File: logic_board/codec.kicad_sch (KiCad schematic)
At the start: 1 part, among them U2 WM8904CGEFL/V

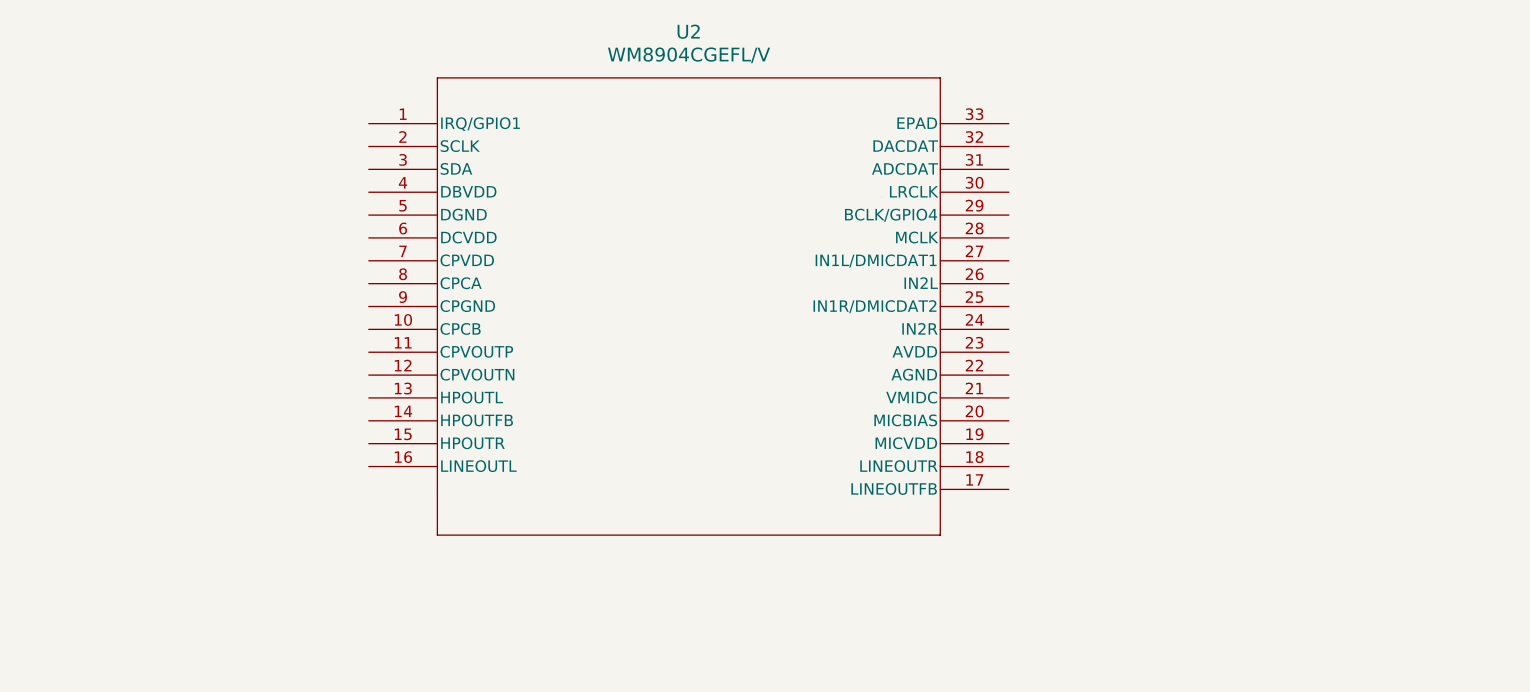
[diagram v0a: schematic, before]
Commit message: Create a pin mapping file
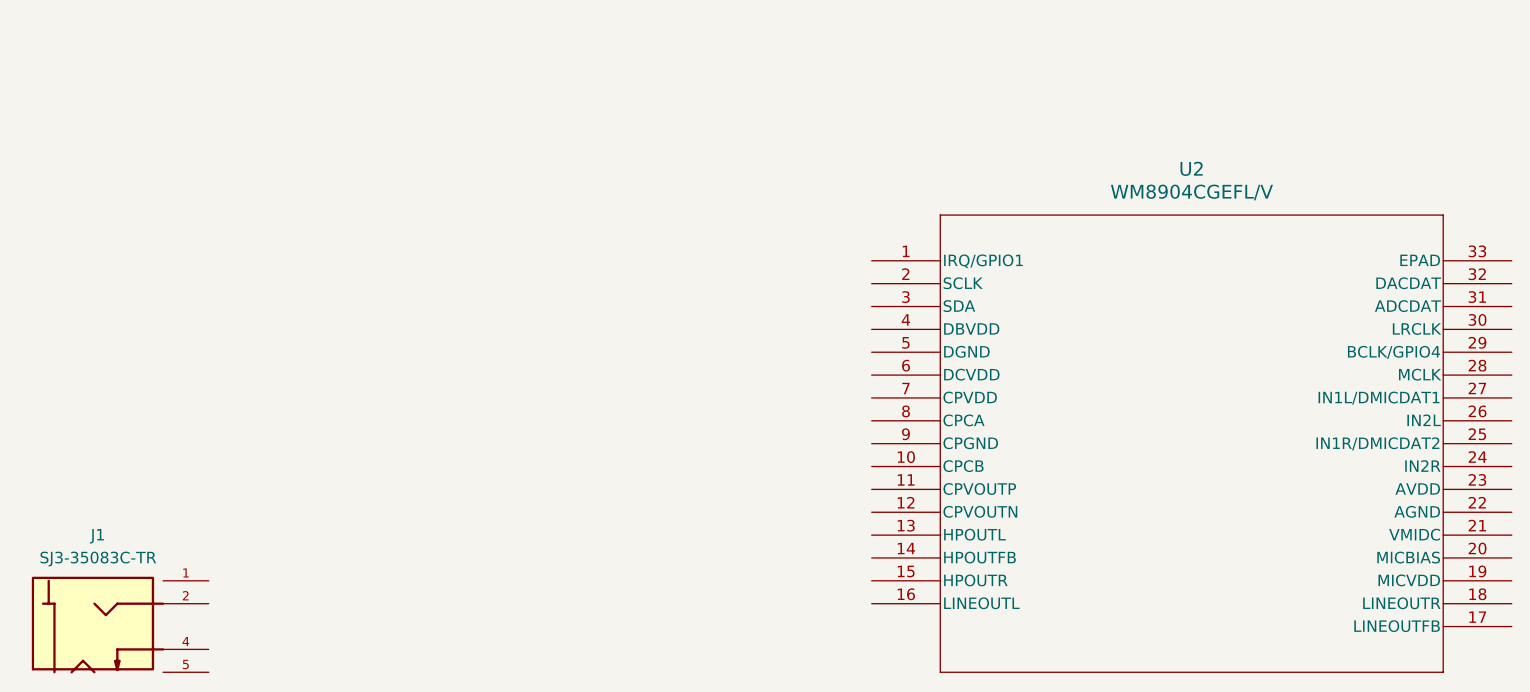
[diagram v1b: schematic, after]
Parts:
- added J1: SJ3-35083C-TR, Custom_Footprints:SAMESKY_SJ3-35083C-TR, symbol Custom_Symbols:SJ3-35083C-TR
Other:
- moved on the sheet: U2
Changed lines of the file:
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@@
 	(paper "A4")
 	(symbol
+		(lib_id "Custom_Symbols:SJ3-35083C-TR")
+		(at 49.53 109.22 0)
+		(unit 1)
+		(exclude_from_sim no)
+		(in_bom no)
+		(on_board yes)
+		(dnp no)
+		(fields_autoplaced yes)
+		(property "Reference" "J1"
+			(at 47.3834 99.06 0)
+			(effects
+				(font
+					(size 1.27 1.27)
+				)
+			)
+		)
+		(property "Value" "SJ3-35083C-TR"
+			(at 47.3834 101.6 0)
+			(effects
+				(font
+					(size 1.27 1.27)
+				)
+			)
+		)
+		(property "Footprint" "Custom_Footprints:SAMESKY_SJ3-35083C-TR"
+			(at 49.53 109.22 0)
+			(effects
+				(font
+					(size 1.27 1.27)
+				)
+				(justify bottom)
+				(hide yes)
+			)
+		)
+		(property "Datasheet" "https://www.sameskydevices.com/product/resource/sj3-3508x.pdf"
+			(at 49.53 109.22 0)
+			(effects
+				(font
+					(size 1.27 1.27)
+				)
+				(hide yes)
+			)
+		)
+		(property "Description" "3.5mm Audio Jack"
+			(at 49.53 109.22 0)
+			(effects
+				(font
+					(size 1.27 1.27)
+				)
+				(hide yes)
+			)
+		)
+		(property "PARTREV" "1.01"
+			(at 49.53 109.22 0)
+			(effects
+				(font
+					(size 1.27 1.27)
+				)
+				(justify bottom)
+				(hide yes)
+			)
+		)
+		(property "STANDARD" "Manufacturer Recommendations"
+			(at 49.53 109.22 0)
+			(effects
+				(font
+					(size 1.27 1.27)
+				)
+				(justify bottom)
+				(hide yes)
+			)
+		)
+		(property "MAXIMUM_PACKAGE_HEIGHT" "5.3mm"
+			(at 49.53 109.22 0)
+			(effects
+				(font
+					(size 1.27 1.27)
+				)
+				(justify bottom)
+				(hide yes)
+			)
+		)
+		(property "MANUFACTURER" "Same Sky"
+			(at 49.53 109.22 0)
+			(effects
+				(font
+					(size 1.27 1.27)
+				)
+				(justify bottom)
+				(hide yes)
+			)
+		)
+		(pin "1"
+		)
+		(pin "2"
+		)
+		(pin "4"
+		)
+		(pin "5"
+		)
+		(instances
+			(project "logic_board"
+				(path "/b7b37fe1-b409-497a-9440-d94d882f6459/824f357b-6dd3-4dc3-a0f3-1ff6a8c5aeec"
+					(reference "J1")
+					(unit 1)
+				)
+			)
+		)
+	)
+	(symbol
 		(lib_id "Custom_Symbols:WM8904CGEFL_V")
-		(at 77.47 53.34 0)
+		(at 133.35 68.58 0)
 		(unit 1)
 		(exclude_from_sim no)
@@
 		(fields_autoplaced yes)
 		(property "Reference" "U2"
-			(at 113.03 43.18 0)
+			(at 168.91 58.42 0)
 			(effects
 				(font
@@
 		)
 		(property "Value" "WM8904CGEFL/V"
-			(at 113.03 45.72 0)
+			(at 168.91 60.96 0)
 			(effects
 				(font
@@
 		)
 		(property "Footprint" "Custom_Footprints:QFN32_4X4_CIR"
-			(at 77.47 53.34 0)
+			(at 133.35 68.58 0)
 			(effects
 				(font
@@
 			)
 		)
-		(property "Datasheet" "WM8904CGEFL/V"
-			(at 77.47 53.34 0)
+		(property "Datasheet" "https://statics.cirrus.com/pubs/proDatasheet/WM8904_Rev4.0.pdf"
+			(at 133.35 68.58 0)
 			(effects
 				(font
@@
 			)
 		)
-		(property "Description" ""
-			(at 77.47 53.34 0)
+		(property "Description" "Audio Codec"
+			(at 133.35 68.58 0)
 			(effects
 				(font
@@
 		)
 		(property "LCSC Part Number" "C1521513"
-			(at 77.47 53.34 0)
+			(at 133.35 68.58 0)
 			(effects
 				(font

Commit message: Add more parts to schematic
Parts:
- added J4: AudioPlug2, Connector_Wire:SolderWire-0.5sqmm_1x02_P4.6mm_D0.9mm_OD2.1mm, symbol Connector_Audio:AudioPlug2
- added U6: TLV9061xDBV, Package_TO_SOT_SMD:SOT-23-5, symbol Amplifier_Operational:TLV9061xDBV
- J1: LCSC Part Number (none) -> C9900193904
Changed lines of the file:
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@@
+			)
+		)
+		(property "LCSC Part Number" "C9900193904"
+			(at 49.53 109.22 0)
+			(effects
+				(font
+					(size 1.27 1.27)
+				)
+				(hide yes)
 			)
 		)
@@
 					(unit 1)
 				)
+			)
+		)
+	)
+	(symbol
+		(lib_id "Connector_Audio:AudioPlug2")
+		(at 35.56 73.66 0)
+		(unit 1)
+		(exclude_from_sim no)
+		(in_bom no)
+		(on_board yes)
+		(dnp no)
+		(fields_autoplaced yes)
+		(property "Reference" "J4"
+			(at 35.56 63.5 0)
+			(effects
+				(font
+					(size 1.27 1.27)
+				)
+			)
+		)
+		(property "Value" "AudioPlug2"
+			(at 35.56 66.04 0)
+			(effects
+				(font
+					(size 1.27 1.27)
+				)
+			)
+		)
+		(property "Footprint" "Connector_Wire:SolderWire-0.5sqmm_1x02_P4.6mm_D0.9mm_OD2.1mm"
+			(at 44.45 74.93 0)
+			(effects
+				(font
+					(size 1.27 1.27)
+				)
+				(hide yes)
+			)
+		)
+		(property "Datasheet" "~"
+			(at 44.45 74.93 0)
+			(effects
+				(font
+					(size 1.27 1.27)
+				)
+				(hide yes)
+			)
+		)
+		(property "Description" "Audio Jack, 2 Poles (Mono / TS)"
+			(at 35.56 73.66 0)
+			(effects
+				(font
+					(size 1.27 1.27)
+				)
+				(hide yes)
+			)
+		)
+		(pin "S"
+		)
+		(pin "T"
+		)
+		(instances
+			(project ""
+				(path "/b7b37fe1-b409-497a-9440-d94d882f6459/824f357b-6dd3-4dc3-a0f3-1ff6a8c5aeec"
+					(reference "J4")
+					(unit 1)
+				)
+			)
+		)
+	)
+	(symbol
+		(lib_id "Amplifier_Operational:TLV9061xDBV")
+		(at 68.58 50.8 0)
+		(unit 1)
+		(exclude_from_sim no)
+		(in_bom yes)
+		(on_board yes)
+		(dnp no)
+		(fields_autoplaced yes)
+		(property "Reference" "U6"
+			(at 81.28 44.3798 0)
+			(effects
+				(font
+					(size 1.27 1.27)
+				)
+			)
+		)
+		(property "Value" "TLV9061xDBV"
+			(at 81.28 46.9198 0)
+			(effects
+				(font
+					(size 1.27 1.27)
+				)
+			)
+		)
+		(property "Footprint" "Package_TO_SOT_SMD:SOT-23-5"
+			(at 53.34 69.85 0)
+			(effects
+				(font
+					(size 1.27 1.27)
+				)
+				(justify left)
+				(hide yes)
+			)
+		)
+		(property "Datasheet" "https://www.ti.com/lit/ds/symlink/tlv9061.pdf"
+			(at 68.58 30.48 0)
+			(effects
+				(font
+					(size 1.27 1.27)
+				)
+				(hide yes)
+			)
+		)
+		(property "Description" "10-MHz, RRIO, CMOS Operational Amplifiers for Cost-Sensitive Systems, SOT-23-5"
+			(at 68.58 50.8 0)
+			(effects
+				(font
+					(size 1.27 1.27)
+				)
+				(hide yes)
+			)
+		)
+		(property "LCSC Part Number" "C398358"
+			(at 68.58 50.8 0)
+			(effects
+				(font
+					(size 1.27 1.27)
+				)
+				(hide yes)
+			)
+		)
+		(pin "1"
+		)
+		(pin "3"
+		)
+		(pin "5"
+		)
+		(pin "4"
+		)
+		(pin "2"
+		)
+		(instances
+			(project ""
+				(path "/b7b37fe1-b409-497a-9440-d94d882f6459/824f357b-6dd3-4dc3-a0f3-1ff6a8c5aeec"
+					(reference "U6")
+					(unit 1)
+				)

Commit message: Board and symbol updates.
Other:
- moved on the sheet: J4, U6
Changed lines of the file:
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@@
 	(symbol
 		(lib_id "Custom_Symbols:SJ3-35083C-TR")
-		(at 49.53 109.22 0)
+		(at 80.01 107.95 0)
 		(unit 1)
 		(exclude_from_sim no)
@@
 		(fields_autoplaced yes)
 		(property "Reference" "J1"
-			(at 47.3834 99.06 0)
+			(at 77.8634 97.79 0)
 			(effects
 				(font
@@
 		)
 		(property "Value" "SJ3-35083C-TR"
-			(at 47.3834 101.6 0)
+			(at 77.8634 100.33 0)
 			(effects
 				(font
@@
 		)
 		(property "Footprint" "Custom_Footprints:SAMESKY_SJ3-35083C-TR"
-			(at 49.53 109.22 0)
+			(at 80.01 107.95 0)
 			(effects
 				(font
@@
 		)
 		(property "Datasheet" "https://www.sameskydevices.com/product/resource/sj3-3508x.pdf"
-			(at 49.53 109.22 0)
+			(at 80.01 107.95 0)
 			(effects
 				(font
@@
 		)
 		(property "Description" "3.5mm Audio Jack"
-			(at 49.53 109.22 0)
+			(at 80.01 107.95 0)
 			(effects
 				(font
@@
 		)
 		(property "PARTREV" "1.01"
-			(at 49.53 109.22 0)
+			(at 80.01 107.95 0)
 			(effects
 				(font
@@
 		)
 		(property "STANDARD" "Manufacturer Recommendations"
-			(at 49.53 109.22 0)
+			(at 80.01 107.95 0)
 			(effects
 				(font
@@
 		)
 		(property "MAXIMUM_PACKAGE_HEIGHT" "5.3mm"
-			(at 49.53 109.22 0)
+			(at 80.01 107.95 0)
 			(effects
 				(font
@@
 		)
 		(property "MANUFACTURER" "Same Sky"
-			(at 49.53 109.22 0)
+			(at 80.01 107.95 0)
 			(effects
 				(font
@@
 		)
 		(property "LCSC Part Number" "C9900193904"
-			(at 49.53 109.22 0)
+			(at 80.01 107.95 0)
 			(effects
 				(font
@@
 	(symbol
 		(lib_id "Connector_Audio:AudioPlug2")
-		(at 35.56 73.66 0)
+		(at 40.64 59.69 0)
 		(unit 1)
 		(exclude_from_sim no)
@@
 		(fields_autoplaced yes)
 		(property "Reference" "J4"
-			(at 35.56 63.5 0)
+			(at 40.64 49.53 0)
 			(effects
 				(font
@@
 		)
 		(property "Value" "AudioPlug2"
-			(at 35.56 66.04 0)
+			(at 40.64 52.07 0)
 			(effects
 				(font
@@
 		)
 		(property "Footprint" "Connector_Wire:SolderWire-0.5sqmm_1x02_P4.6mm_D0.9mm_OD2.1mm"
-			(at 44.45 74.93 0)
+			(at 49.53 60.96 0)
 			(effects
 				(font
@@
 		)
 		(property "Datasheet" "~"
-			(at 44.45 74.93 0)
+			(at 49.53 60.96 0)
 			(effects
 				(font
@@
 		)
 		(property "Description" "Audio Jack, 2 Poles (Mono / TS)"
-			(at 35.56 73.66 0)
+			(at 40.64 59.69 0)
 			(effects
 				(font
@@
 	(symbol
 		(lib_id "Amplifier_Operational:TLV9061xDBV")
-		(at 68.58 50.8 0)
+		(at 77.47 58.42 0)
 		(unit 1)
 		(exclude_from_sim no)
@@
 		(fields_autoplaced yes)
 		(property "Reference" "U6"
-			(at 81.28 44.3798 0)
+			(at 90.17 51.9998 0)
 			(effects
 				(font
@@
 		)
 		(property "Value" "TLV9061xDBV"
-			(at 81.28 46.9198 0)
+			(at 90.17 54.5398 0)
 			(effects
 				(font
@@
 		)
 		(property "Footprint" "Package_TO_SOT_SMD:SOT-23-5"
-			(at 53.34 69.85 0)
+			(at 62.23 77.47 0)
 			(effects
 				(font
@@
 		)
 		(property "Datasheet" "https://www.ti.com/lit/ds/symlink/tlv9061.pdf"
-			(at 68.58 30.48 0)
+			(at 77.47 38.1 0)
 			(effects
 				(font
@@
 		)
 		(property "Description" "10-MHz, RRIO, CMOS Operational Amplifiers for Cost-Sensitive Systems, SOT-23-5"
-			(at 68.58 50.8 0)
+			(at 77.47 58.42 0)
 			(effects
 				(font
@@
 		)
 		(property "LCSC Part Number" "C398358"
-			(at 68.58 50.8 0)
-			(effects
-				(font
+			(at 77.47 58.42 0)
+			(effects
+				(font

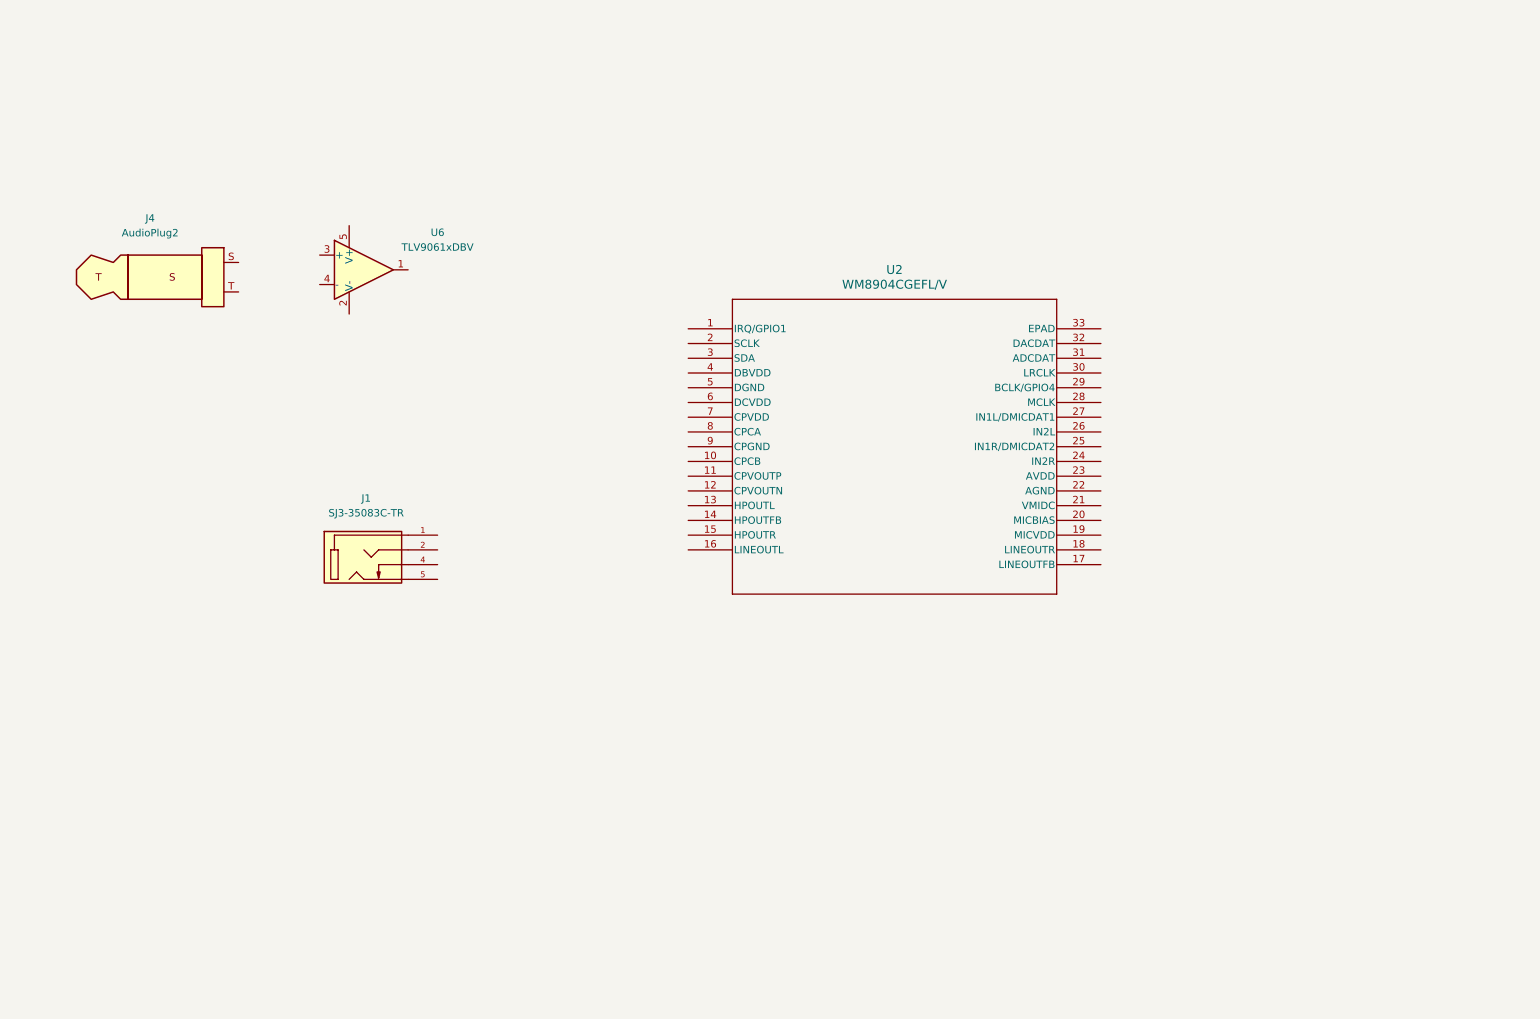
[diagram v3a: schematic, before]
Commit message: Ready for routing. - Lay out all components in proper positions - Add all support passives (bypass caps, etc) - Add board corner cutouts for enclosure bosses.
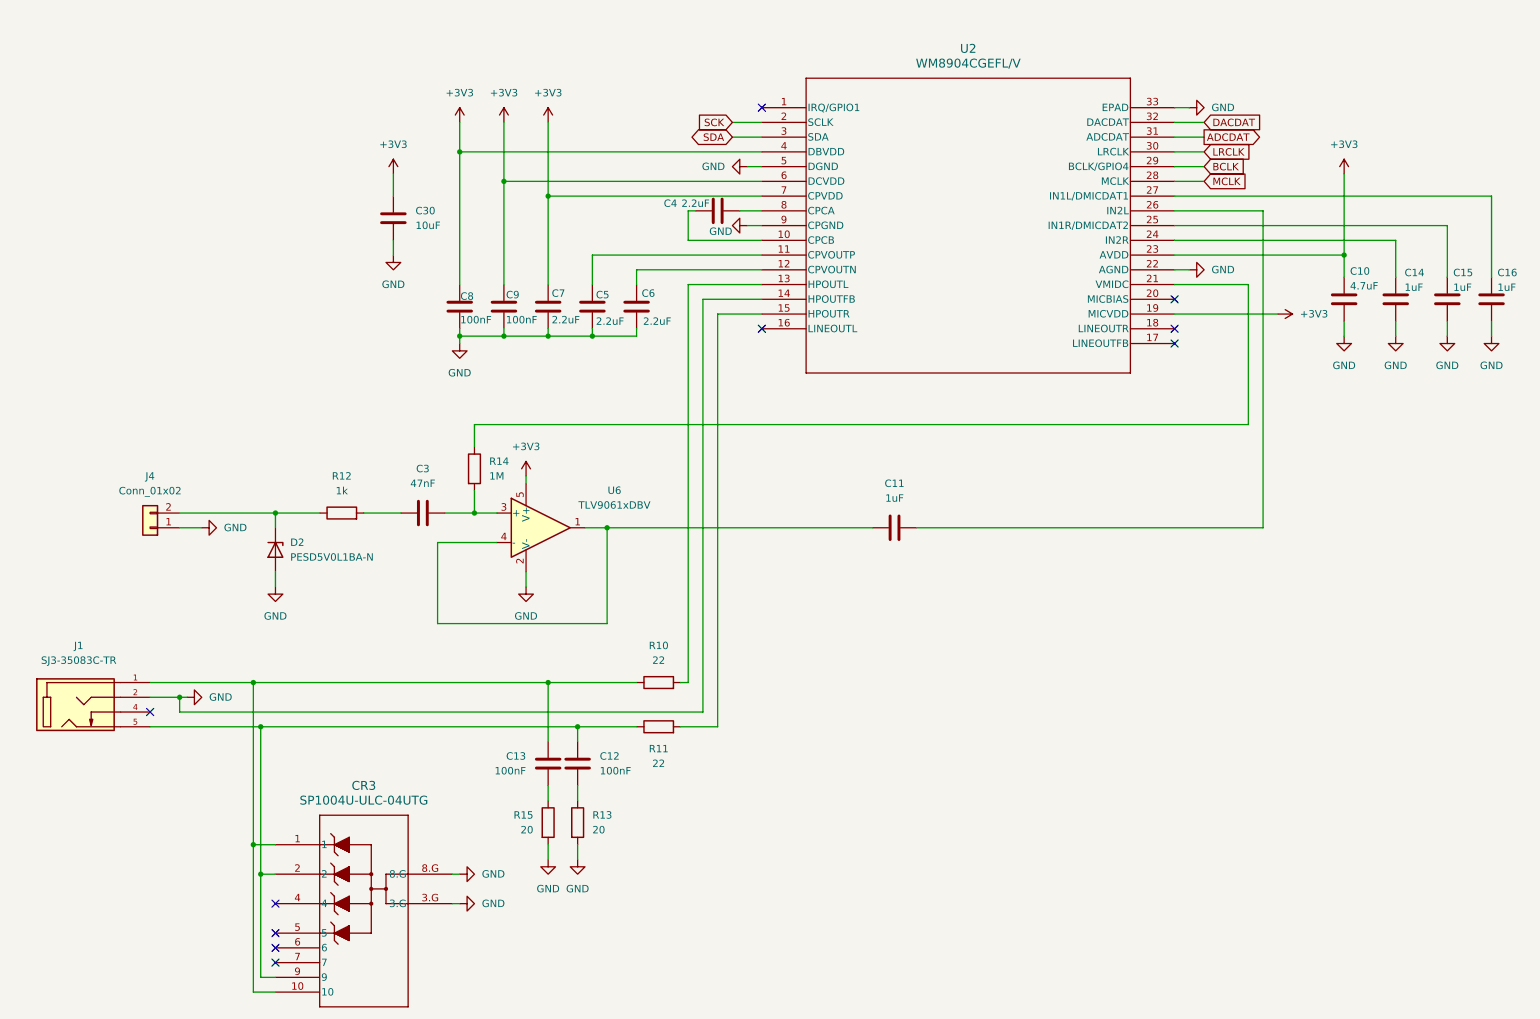
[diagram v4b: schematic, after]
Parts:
- removed J4: AudioPlug2, Connector_Wire:SolderWire-0.5sqmm_1x02_P4.6mm_D0.9mm_OD2.1mm, symbol Connector_Audio:AudioPlug2
- added C10: 4.7uF, Capacitor_SMD:C_0603_1608Metric, symbol Device:C
- added C11, C14, C15, C16: 1uF, Capacitor_SMD:C_0603_1608Metric, symbol Device:C
- added C12, C13, C8, C9: 100nF, Capacitor_SMD:C_0603_1608Metric, symbol Device:C
- added C3: 47nF, Capacitor_SMD:C_0603_1608Metric, symbol Device:C
- added C30: 10uF, Capacitor_SMD:C_0603_1608Metric, symbol Device:C
- added C4, C5, C6, C7: 2.2uF, Capacitor_SMD:C_0603_1608Metric, symbol Device:C
- added CR3: SP1004U-ULC-04UTG, Custom_Footprints:1004DFN_LTF, symbol Custom_Symbols:SP1004U-ULC-04UTG
- added D2: PESD5V0L1BA-N, Diode_SMD:D_SOD-323F, symbol Diode:PESD5V0L1UL
- added J4: Conn_01x02, Connector_Wire:SolderWire-0.1sqmm_1x02_P3.6mm_D0.4mm_OD1mm, symbol Connector_Generic:Conn_01x02
- added R10, R11: 22, Resistor_SMD:R_0603_1608Metric, symbol Device:R
- added R12: 1k, Resistor_SMD:R_0603_1608Metric, symbol Device:R
- added R13, R15: 20, Resistor_SMD:R_0603_1608Metric, symbol Device:R
- added R14: 1M, Resistor_SMD:R_0603_1608Metric, symbol Device:R
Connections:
- net at J1.1: now also C13.1, CR3.1, CR3.10, R10.1
- net GND: now reaches J1.2
- net GND: now also U2.14 (HPOUTFB), U2.22 (AGND), U2.33 (EPAD), U2.5 (DGND), U2.9 (CPGND), U6.2 (V-), C10.1, C14.1, C15.1, C16.1, C30.2, C5.2, C6.2, C7.2, C8.2, C9.2, CR3.3.G, CR3.8.G, D2.2 (A), J4.1 (Pin_1), R13.2, R15.2
- net at J1.5: now also C12.1, CR3.2, CR3.9, R11.1
- net at U6.1: now also U6.4 (-), C11.1
- net at U6.3 (+): now also C3.2, R14.2
- net +3V3: now reaches U6.5 (V+)
- net +3V3: now also U2.19 (MICVDD), U2.23 (AVDD), U2.4 (DBVDD), U2.6 (DCVDD), U2.7 (CPVDD), C10.2, C30.1, C7.1, C8.1, C9.1
- net at U2.10 (CPCB): now also C4.2
- net at U2.11 (CPVOUTP): now also C5.1
- net at U2.12 (CPVOUTN): now also C6.1
- net at U2.13 (HPOUTL): now also R10.2
- net at U2.15 (HPOUTR): now also R11.2
- net SCK: now reaches U2.2 (SCLK)
- net at U2.21 (VMIDC): now also R14.1
- net at U2.24 (IN2R): now also C14.2
- net at U2.25 (IN1R/DMICDAT2): now also C15.2
- net at U2.26 (IN2L): now also C11.2
- net at U2.27 (IN1L/DMICDAT1): now also C16.2
- net MCLK: now reaches U2.28 (MCLK)
- net BCLK: now reaches U2.29 (BCLK/GPIO4)
- net SDA: now reaches U2.3 (SDA)
- net LRCLK: now reaches U2.30 (LRCLK)
- net ADCDAT: now reaches U2.31 (ADCDAT)
- net DACDAT: now reaches U2.32 (DACDAT)
- net at U2.8 (CPCA): now also C4.1
- new net: C13.2, R15.1
- new net: C3.1, R12.2
- new net: C12.2, R13.1
- new net: D2.1 (K), J4.2 (Pin_2), R12.1
- no-connect marks 0 -> 10
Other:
- moved on the sheet: J1, U2, U6
